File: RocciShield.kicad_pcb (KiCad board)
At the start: 2 copper layers, 99.6 x 53.8 mm, 195 parts, among them J1 Battery, J10 M3, J11 I2C6, J12 Power, J13 M2, J14 I2C7, J2 I2C0, J3 I2C1, J4 I2C2, J5 I2C3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

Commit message: layout ready for review
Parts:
- moved TP21 17.0 mm to (121.2, 108.0), turned to 0 degrees
- moved TP19 17.0 mm to (121.2, 101.6), turned to 0 degrees
- moved TP20 16.4 mm to (121.5, 97.8), turned to 0 degrees
- moved TP22 16.4 mm to (121.5, 104.7), turned to 0 degrees
- moved TP17 16.0 mm to (122.0, 115.8), turned to 0 degrees
- moved TP18 16.0 mm to (122.0, 112.8), turned to 0 degrees
- moved TP16 15.3 mm to (122.6, 120.8), turned to 0 degrees
- moved TP15 15.2 mm to (122.7, 123.2), turned to 0 degrees
- moved R60 13.6 mm to (123.7, 110.3), turned to 0 degrees
- moved R45 13.5 mm to (123.6, 118.1), turned to 0 degrees
- moved R37 13.5 mm to (123.6, 125.9), turned to 0 degrees
- moved J10 12.9 mm to (135.1, 98.1), turned to 0 degrees
- moved J6 12.9 mm to (135.1, 120.9), turned to 0 degrees
- moved J8 12.9 mm to (135.1, 113.3), turned to 0 degrees
- moved J13 12.9 mm to (135.1, 105.7), turned to 0 degrees
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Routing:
- net M3_IN1: track 28.2 -> 47.3 mm
- net M0_IN1: track 66.3 -> 84.9 mm
- net M1_IN1: track 52.6 -> 70.9 mm
- net M2_IN1: track 40.7 -> 58.1 mm
- net M3_IN2: track 32.7 -> 46.6 mm
- net M2_IN2: track 44.1 -> 57.6 mm
- net +12V: track 114.5 -> 127.9 mm, vias 5 -> 6
- net M1_IN2: track 58.7 -> 71.8 mm
- net M0_IN2: track 71.2 -> 84.2 mm
- net Net-(U8-ILIM): track 2.01 -> 8.89 mm
- net +8V: track 62.5 -> 69.0 mm
- net I2C_RESET: track 112.9 -> 117.8 mm
- net ERROR_LED: track 45.2 -> 48.9 mm
- net GND: track 13.5 -> 10.5 mm, vias 171 -> 142
- net +12VA: track 169.8 -> 172.2 mm
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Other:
- board text added: "- +"
- board text added: "TP4"
- board text removed: "+ -"
- board text removed: "R_VCC"

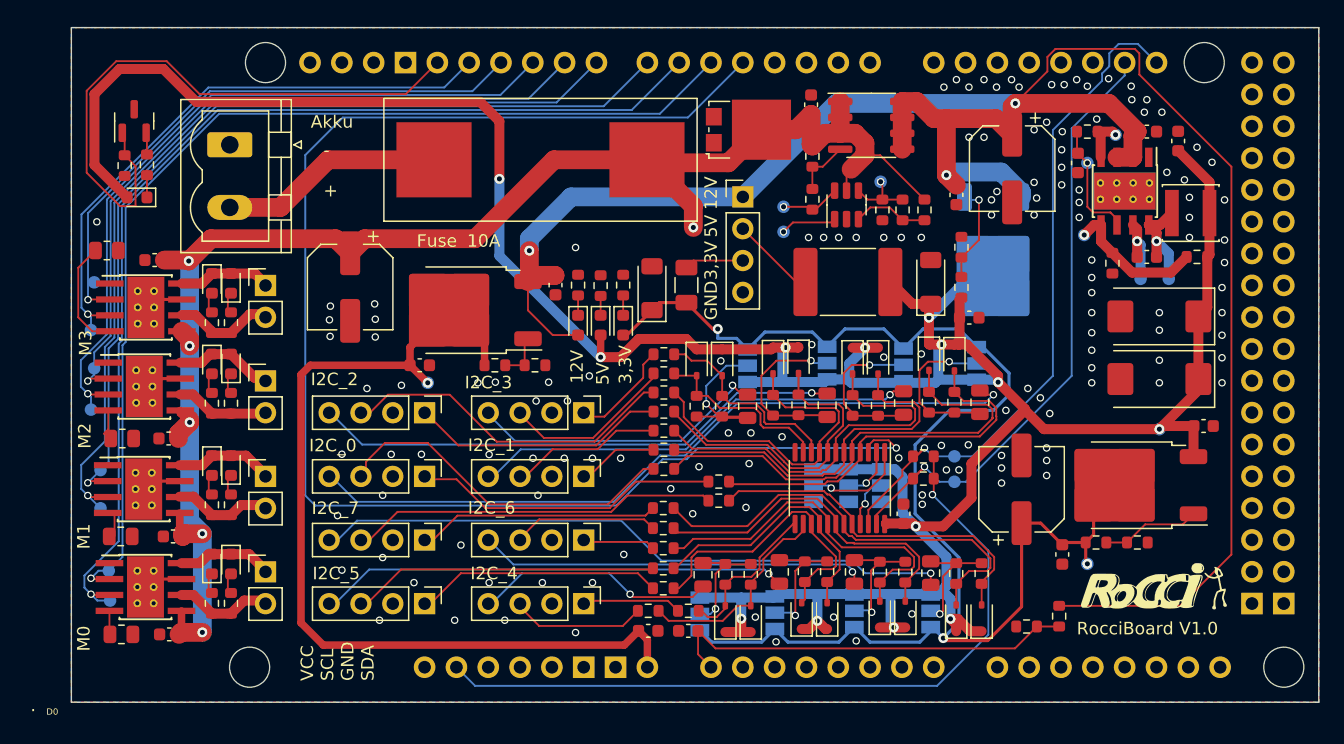
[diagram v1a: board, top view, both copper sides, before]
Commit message: changed i2c order
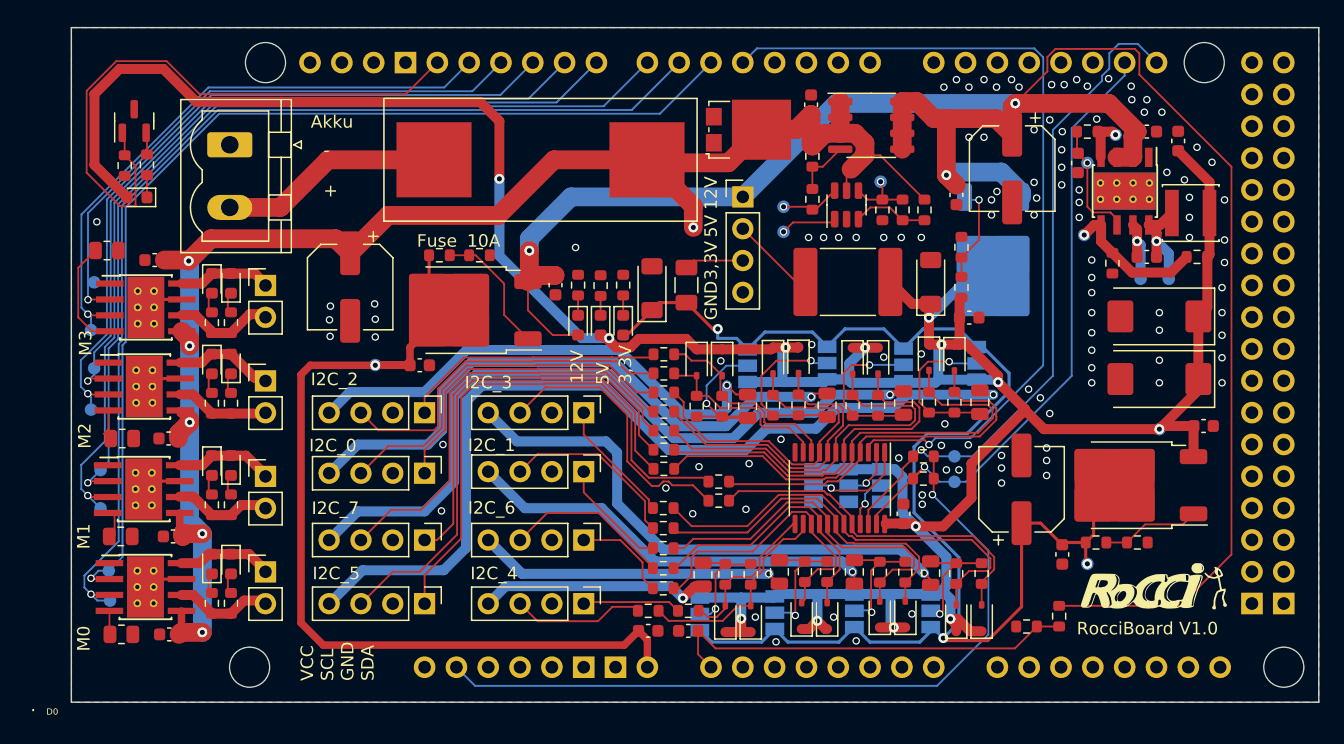
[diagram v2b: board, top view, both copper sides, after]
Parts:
- moved J14 16.3 mm to (160.5, 108.2)
- moved J3 13.7 mm to (147.8, 118.4)
- moved J9 13.7 mm to (160.5, 118.4)
- moved J5 12.7 mm to (147.8, 108.2)
- moved J2 10.2 mm to (147.8, 123.5)
- moved R21 9.84 mm to (149.0, 95.6)
- moved R25 9.84 mm to (152.2, 95.6)
- moved J11 5.46 mm to (160.5, 112.9)
- moved J4 4.83 mm to (147.8, 113.0)
- moved TP12 4.42 mm to (143.9, 104.4)
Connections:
- net Net-(J11-Pin_4) renamed /VCC_I2C6
- net Net-(J14-Pin_4) renamed /VCC_I2C7
- net Net-(J2-Pin_4) renamed /VCC_I2C0
- net Net-(J3-Pin_4) renamed /VCC_I2C1
- net Net-(J4-Pin_4) renamed /VCC_I2C2
- net Net-(J5-Pin_4) renamed /VCC_I2C3
- net Net-(J7-Pin_4) renamed /VCC_I2C4
- net Net-(J9-Pin_4) renamed /VCC_I2C5
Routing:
- net I2C_RESET: track 117.8 -> 66.8 mm
- net Net-(J3-Pin_1): track 6.35 -> 33.3 mm
- net Net-(J3-Pin_3): track 12.1 -> 35.4 mm
- net /VCC_I2C1: track 35.9 -> 59.0 mm
- net Net-(J2-Pin_1): track 24.1 -> 43.3 mm
- net /VCC_I2C3: track 23.6 -> 39.9 mm
- net Net-(J5-Pin_3): track 13.5 -> 28.4 mm
- net /VCC_I2C0: track 58.1 -> 72.2 mm
- net Net-(J2-Pin_3): track 28.2 -> 42.0 mm
- net Net-(J5-Pin_1): track 8.05 -> 21.0 mm
- net /VCC_I2C5: track 37.2 -> 24.7 mm
- net Net-(J9-Pin_1): track 19.4 -> 7.85 mm
- net Net-(J9-Pin_3): track 24.1 -> 13.4 mm
- net Net-(J14-Pin_1): track 18.8 -> 9.90 mm
- net /VCC_I2C7: track 50.9 -> 43.6 mm
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
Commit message: aligned components
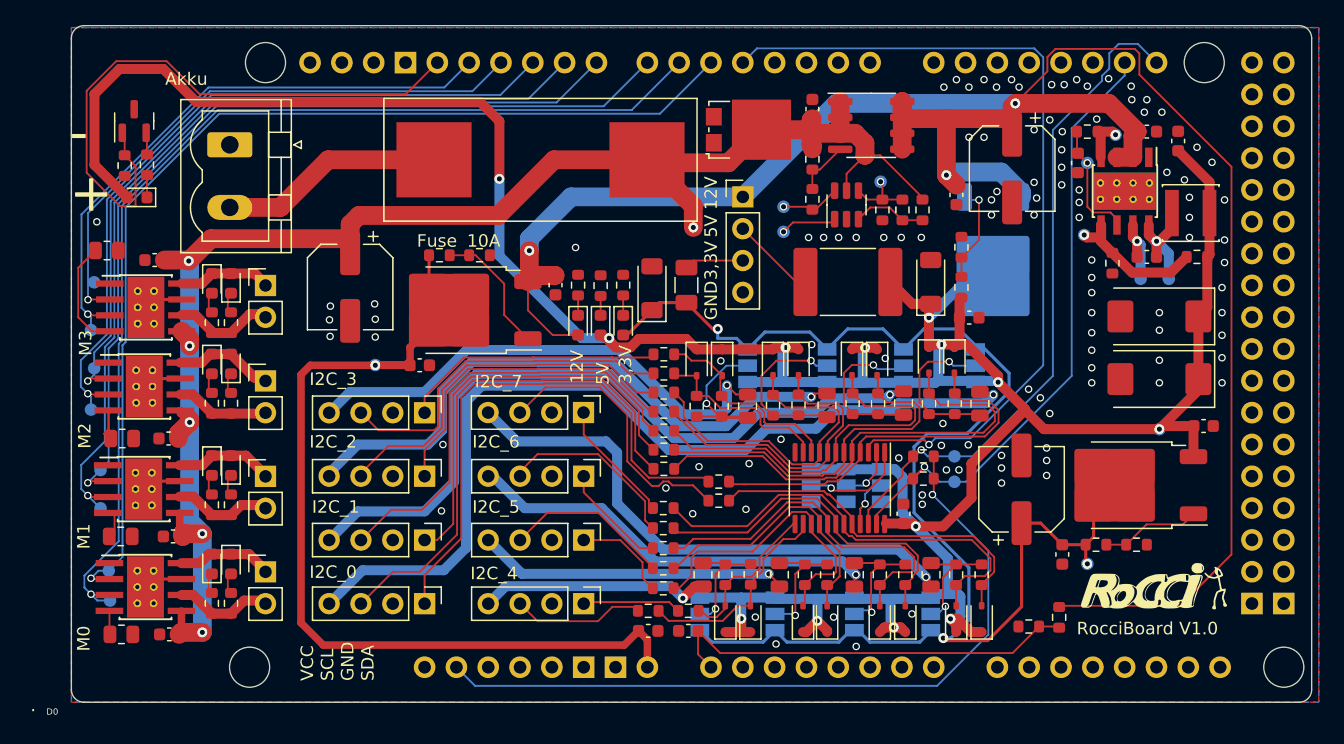
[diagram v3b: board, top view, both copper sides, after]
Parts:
- moved G*** 4.14 mm to (146.5, 93.5)
- moved C8 0.37 mm to (178.8, 84.0)
- moved D24 0.37 mm to (186.2, 124.7)
- moved D25 0.37 mm to (184.2, 124.7)
- moved J11 0.37 mm to (160.5, 113.3)
- moved D21 0.26 mm to (178.0, 124.7)
- moved JP10 0.25 mm to (182.1, 124.3)
- moved JP11 0.25 mm to (188.2, 124.3)
- moved R46 0.24 mm to (178.2, 121.1)
- moved R47 0.24 mm to (180.0, 121.1)
- moved D20 0.24 mm to (180.0, 124.7)
- moved J4 0.24 mm to (147.8, 113.3)
- moved F7 0.23 mm to (176.1, 121.1)
- moved R14 0.23 mm to (178.8, 88.0)
- moved F8 0.23 mm to (182.1, 121.1)
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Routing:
- net +5V: track 261.1 -> 264.2 mm
- net +12V: track 127.9 -> 130.0 mm
- net +12VA: track 172.2 -> 173.8 mm
- net +3V3: track 113.7 -> 114.8 mm
- net /FB: track 11.4 -> 12.1 mm
- net /SW: track 8.45 -> 9.17 mm
- net GND: vias 111 -> 110
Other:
- board size 99.6 x 53.8 mm -> 99 x 54 mm
